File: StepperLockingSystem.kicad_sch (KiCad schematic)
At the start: 23 parts, among them J2 DigitalLED, J9 PowerConnector, U3 TC1185, U4 INA180A1

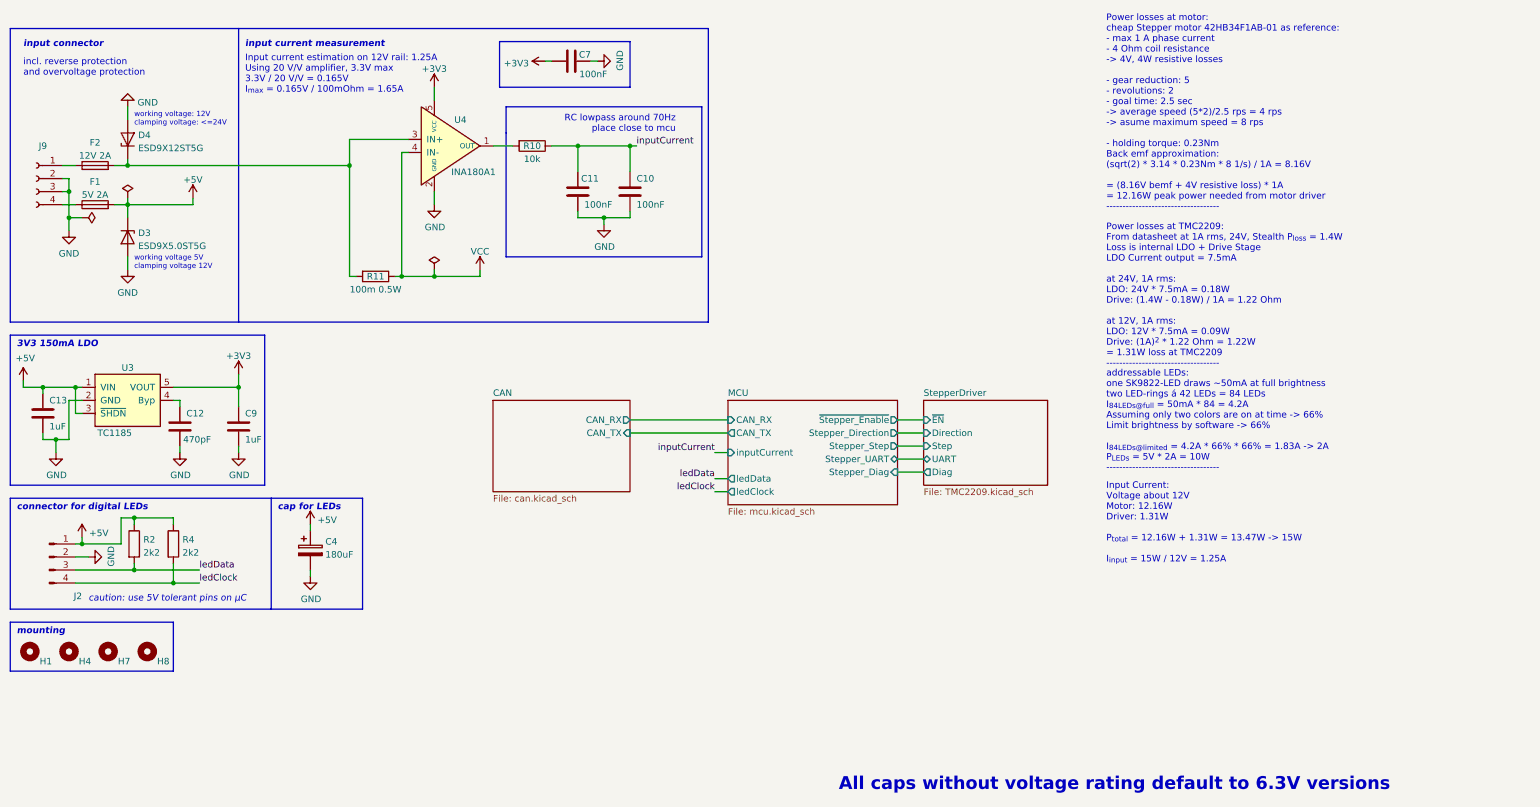
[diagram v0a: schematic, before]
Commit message: Apply suggestions from tux: Single connector for signals Some (better) notes
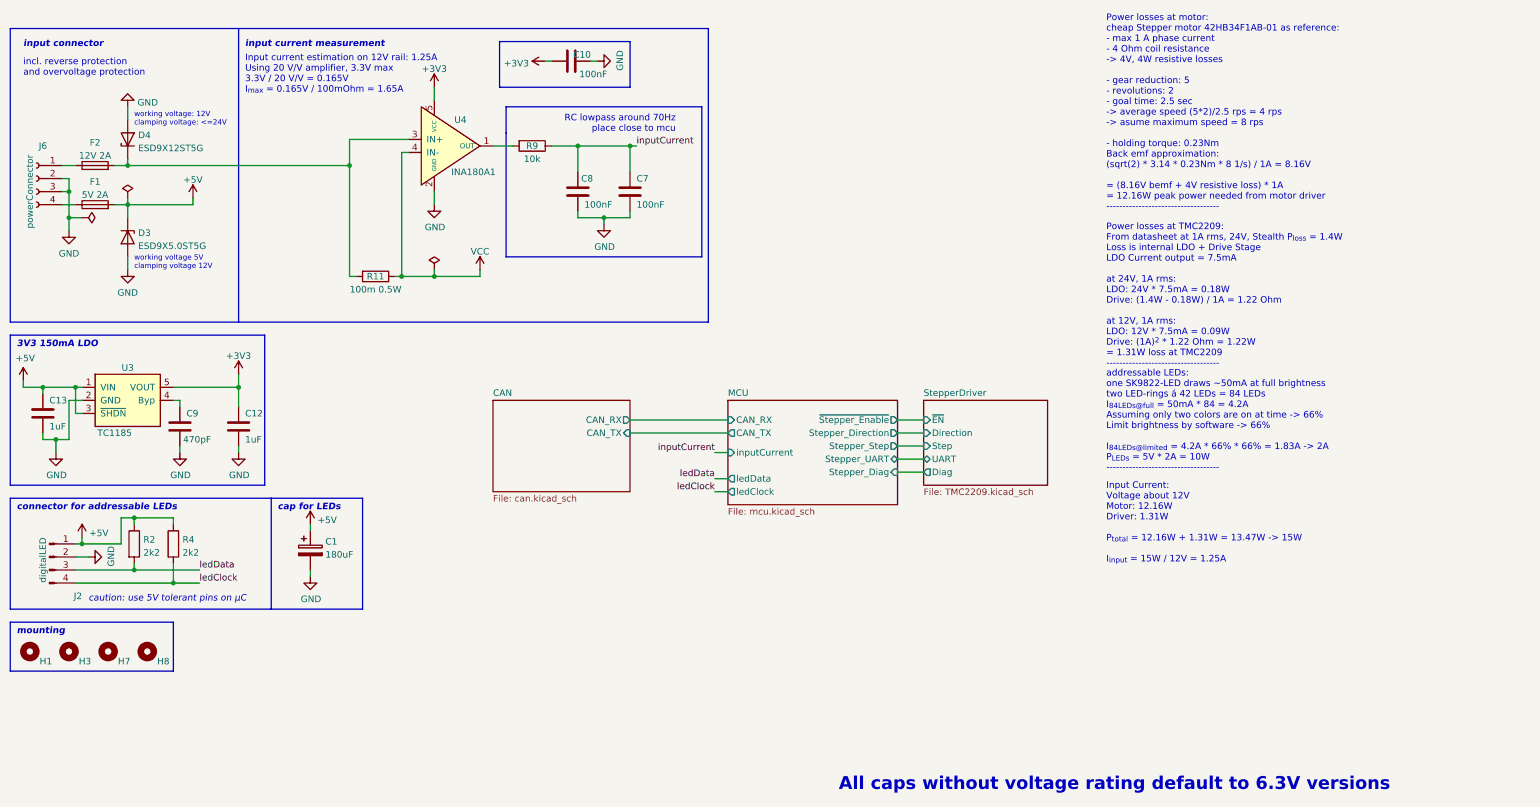
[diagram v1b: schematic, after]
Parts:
- J2: value DigitalLED -> digitalLED
- J6: renamed from J9; value PowerConnector -> powerConnector
- renumbered C4 to C1, C7 to C10, C9 to C12, C10 to C7, C11 to C8, C12 to C9, H4 to H3, R10 to R9
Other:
- note added: "connector for addressable LEDs"
- note removed: "connector for digital LEDs"

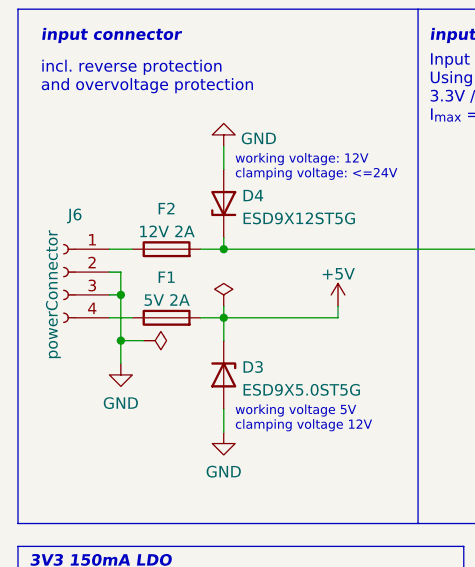
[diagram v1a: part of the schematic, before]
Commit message: Change power input pin out Update exported stuffs Update ReadMe
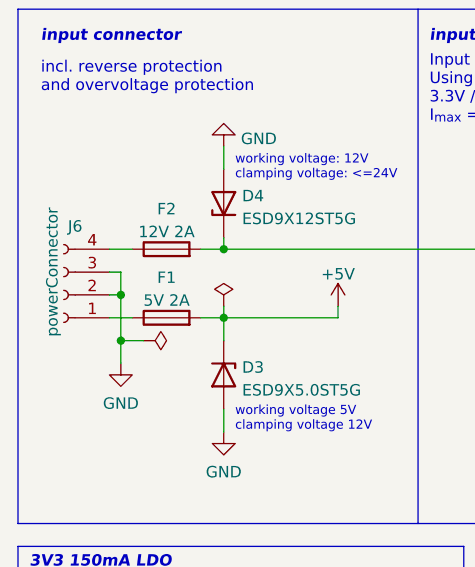
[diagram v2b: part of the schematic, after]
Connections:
- net at J6.1 (Pin_1): now also F1.1; no longer F2.1
- net at J6.4 (Pin_4): now also F2.1; no longer F1.1
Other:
- moved on the sheet: J6
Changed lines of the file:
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@@
     (pin "4")
   )
-  (symbol (lib_id "Connector:Conn_01x04_Female") (at 20.32 45.72 0) (mirror y) (unit 1)
+  (symbol (lib_id "Connector:Conn_01x04_Female") (at 20.32 48.26 180) (unit 1)
     (in_bom yes) (on_board yes)
-    (property "Reference" "J6" (id 0) (at 21.59 39.37 0))
-    (property "Value" "powerConnector" (id 1) (at 19.05 48.26 90))
-    (property "Footprint" "Connector_Phoenix_MSTB:PhoenixContact_MSTBVA_2,5_4-G-5,08_1x04_P5.08mm_Vertical" (id 2) (at 20.32 45.72 0)
+    (property "Reference" "J6" (id 0) (at 21.59 40.64 0))
+    (property "Value" "powerConnector" (id 1) (at 19.05 45.72 90))
+    (property "Footprint" "Connector_Phoenix_MSTB:PhoenixContact_MSTBVA_2,5_4-G-5,08_1x04_P5.08mm_Vertical" (id 2) (at 20.32 48.26 0)
       (effects (font (size 1.27 1.27)) hide)
     )
-    (property "Datasheet" "~" (id 3) (at 20.32 45.72 0)
+    (property "Datasheet" "~" (id 3) (at 20.32 48.26 0)
       (effects (font (size 1.27 1.27)) hide)
     )
